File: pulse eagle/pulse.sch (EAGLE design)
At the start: 26 parts, among them IC1 LM358D, J1 ISP Touch, Y1 8MHz

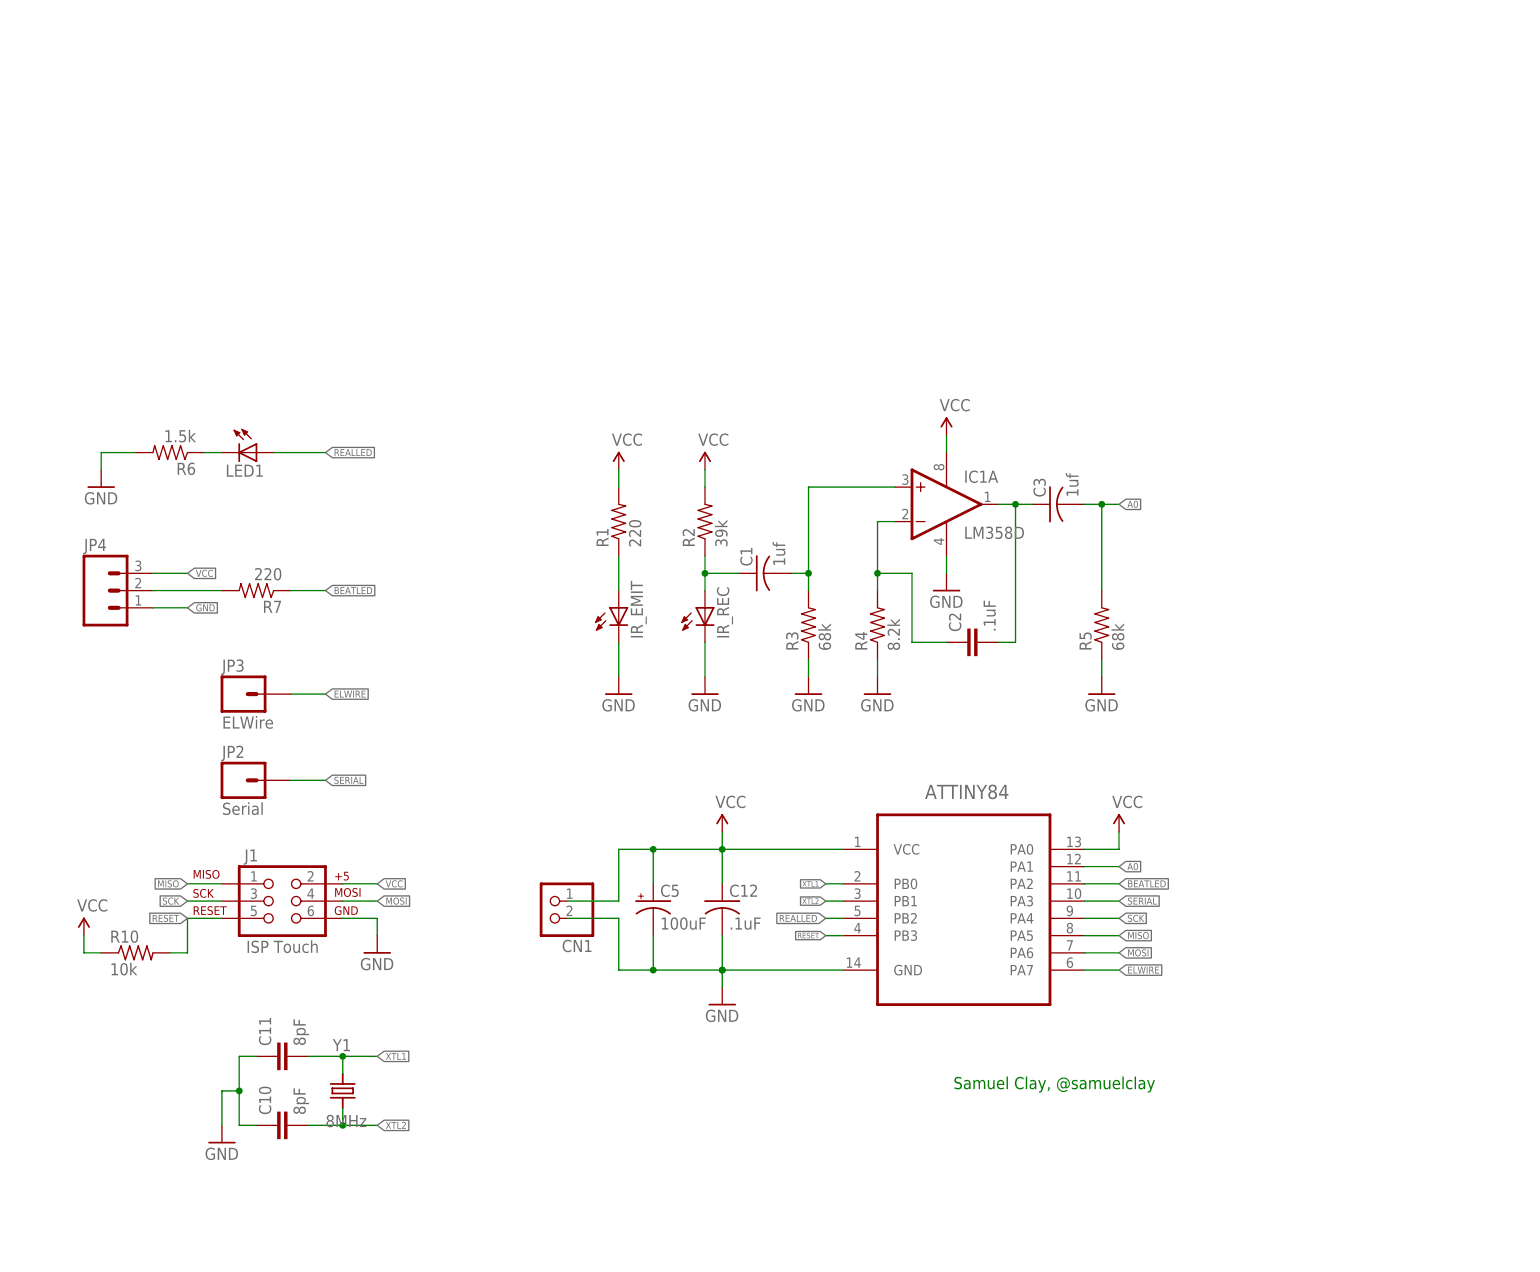
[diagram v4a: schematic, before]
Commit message: Switching from attiny84 to atmega328 for the hardware serial, bigger flash size, additional PWMs, and negligible package size difference.
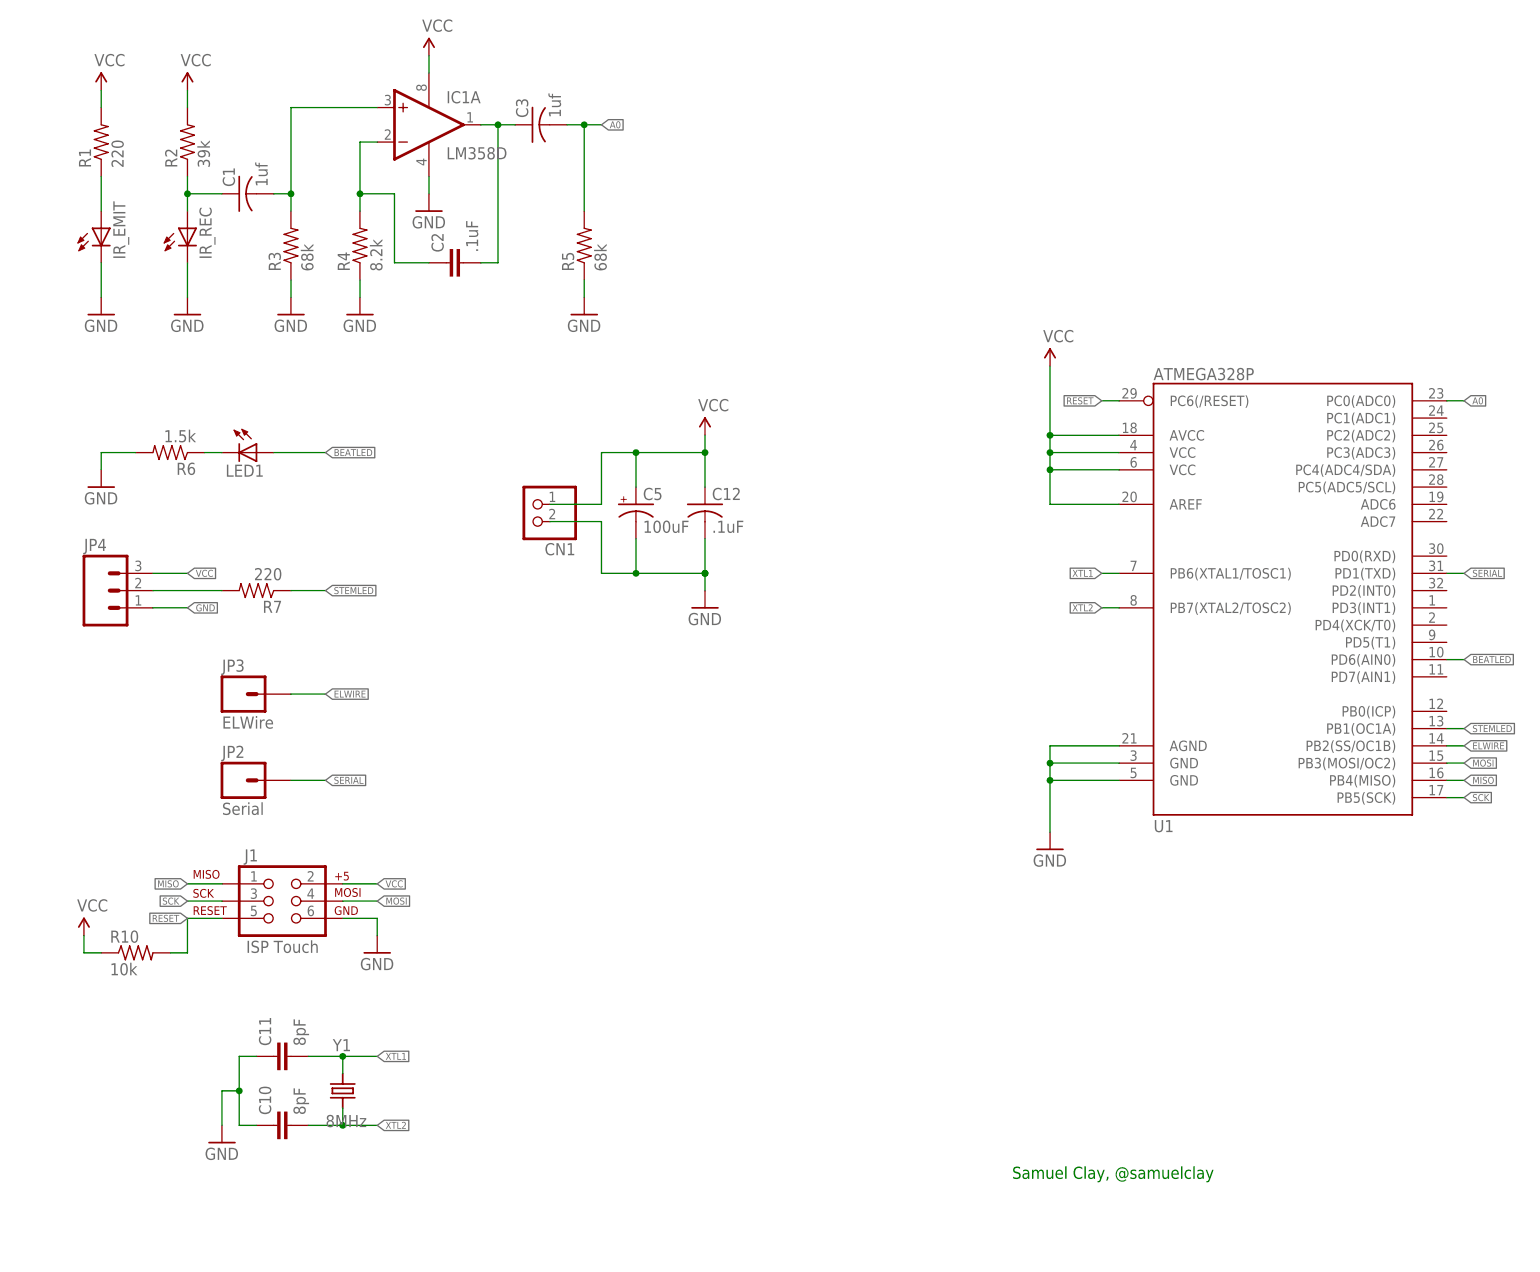
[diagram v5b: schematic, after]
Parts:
- removed ATTINY84: ATTINY84-20SSU, Atmel_By_element14_Batch_1:ATTINY84-20SSU
- added U1: ATMEGA328P, SparkFun-DigitalIC:ATMEGA328_SMT
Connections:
- removed net REALLED: ATTINY84.PB2, LED1.A
- new net STEMLED: R7.1, U1.PB1(OC1A)
- net A0: now also U1.PC0(ADC0); no longer ATTINY84.PA1
- net BEATLED: now also LED1.A, U1.PD6(AIN0); no longer ATTINY84.PA2, R7.1
- net ELWIRE: now also U1.PB2(SS/OC1B); no longer ATTINY84.PA7
- net GND: now also U1.AGND, U1.GND@1, U1.GND@2; no longer ATTINY84.GND
- net MISO: now also U1.PB4(MISO); no longer ATTINY84.PA5
- net MOSI: now also U1.PB3(MOSI/OC2); no longer ATTINY84.PA6
- net RESET: now also U1.PC6(/RESET); no longer ATTINY84.PB3
- net SCK: now also U1.PB5(SCK); no longer ATTINY84.PA4
- net SERIAL: now also U1.PD1(TXD); no longer ATTINY84.PA3
- net VCC: now also U1.AREF, U1.AVCC, U1.VCC@1, U1.VCC@2; no longer ATTINY84.PA0, ATTINY84.VCC
- net XTL1: now also U1.PB6(XTAL1/TOSC1); no longer ATTINY84.PB0
- net XTL2: now also U1.PB7(XTAL2/TOSC2); no longer ATTINY84.PB1
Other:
- moved on the sheet: C1, C12, C2, C3, C5, CN1, IC1A, IR_EMIT, IR_REC, R1, R2, R3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

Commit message: Switch from crappy IR sensors to SI1143 IC.
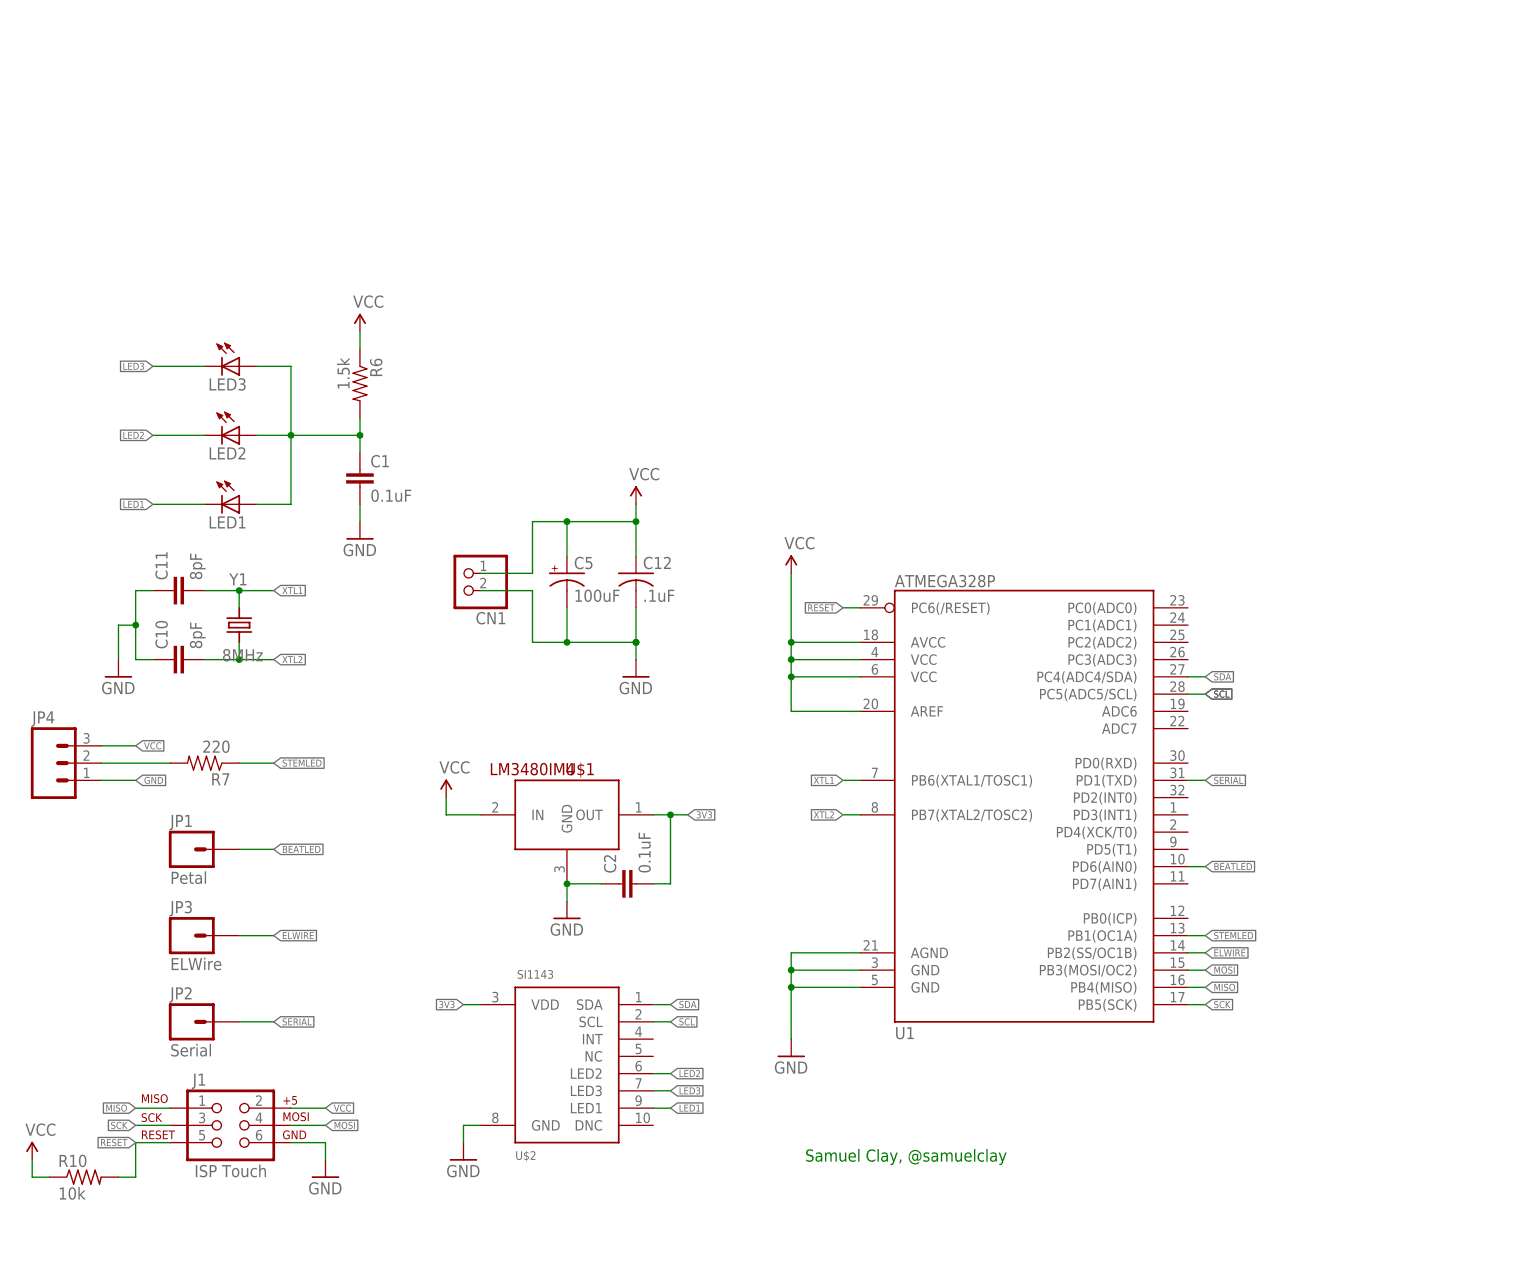
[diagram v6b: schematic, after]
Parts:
- removed C3: 1uf, adafruit:C-USC0805
- removed IC1: LM358D, linear:LM358D
- removed IR_EMIT, IR_REC: (no value), adafruit:LED5MM
- removed R1: 220, SparkFun-Resistors:220-5%
- removed R2: 39k, SparkFun-Resistors:220-5%
- removed R3, R5: 68k, SparkFun-Resistors:220-5%
- removed R4: 8.2k, SparkFun-Resistors:220-5%
- added JP1: Petal, SparkFun-Connectors:M01PTH
- added LED2, LED3: (no value), SparkFun-LED:LED1206
- added U$1: LM3480IM4, SparkFun-PowerIC:LM3480IM4
- added U$2: SI1143, pulse:SI1143
- C1: value 1uf -> 0.1uF; device adafruit:C-USC0805 -> SparkFun-Capacitors:.1UF-CER
- C2: value .1uF -> 0.1uF; device SparkFun-Passives:CAP0805 -> SparkFun-Capacitors:.1UF-CER
- LED1: device SparkFun-LED:LED0603 -> SparkFun-LED:LED1206
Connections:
- removed net A0: C3.2, R5.2, U1.PC0(ADC0)
- removed net N$1: IR_EMIT.A, R1.1
- removed net N$3: C1.2, IC1A.+IN, R3.2
- removed net N$4: C2.1, IC1A.-IN, R4.2
- removed net N$5: C2.2, C3.1, IC1A.OUT
- removed net N$8: LED1.C, R6.1
- new net 3V3: C2.2, U$1.OUT, U$2.VDD
- new net LED1: LED1.C, U$2.LED1
- new net LED2: LED2.C, U$2.LED2
- new net LED3: LED3.C, U$2.LED3
- new net SCL: U$2.SCL, U1.PC5(ADC5/SCL)
- new net SDA: U$2.SDA, U1.PC4(ADC4/SDA)
- net BEATLED: now also JP1.1; no longer LED1.A
- net GND: now also C1.2, C2.1, U$1.GND, U$2.GND; no longer IC1P.V-, IR_EMIT.C, IR_REC.C, R3.1, R4.1, R5.1, R6.2
- net N$2: now also LED1.A, LED2.A, LED3.A, R6.2; no longer IR_REC.A, R2.1
- net VCC: now also R6.1, U$1.IN; no longer IC1P.V+, R1.2, R2.2
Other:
- moved on the sheet: C1, C10, C11, C12, C2, C5, CN1, J1, JP2, JP3, JP4, LED1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

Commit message: Re-orienting and preparing board for layout.
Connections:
- new net INT0: U$2.INT, U1.PD2(INT0)
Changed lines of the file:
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@@
+</segment>
+</net>
+<net name="INT0" class="0">
+<segment>
+<pinref part="U$2" gate="SI1143" pin="INT"/>
+<wire x1="96.52" y1="27.94" x2="99.06" y2="27.94" width="0.1524" layer="91"/>
+<label x="99.06" y="27.94" size="1.016" layer="95" xref="yes"/>
+</segment>
+<segment>
+<pinref part="U1" gate="G$1" pin="PD2(INT0)"/>
+<wire x1="175.26" y1="63.5" x2="177.8" y2="63.5" width="0.1524" layer="91"/>
+<label x="177.8" y="63.5" size="1.016" layer="95" xref="yes"/>
 </segment>
 </net>
